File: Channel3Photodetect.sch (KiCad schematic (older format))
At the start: 7 parts, among them U201 MCP6404, U202 LM339

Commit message: revised feedback resistor and updated reference voltage divider
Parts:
- removed R402: 22M, Resistors_SMD:R_0805_HandSoldering, symbol R_Small
- C401: value 2.2p -> 50p
- R401: value 22M -> 2M; Fieldname (none) -> Value; MPN RMCF0805FT22M0 -> (none)
- renumbered R403 to R402
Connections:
- net at C401.1, R402.2, U201.8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: now also R401.1
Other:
- moved on the sheet: R401
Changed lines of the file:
@@
 P 5540 1890
 F 0 "C401" V 5660 1850 50  0000 L CNN
-F 1 "2.2p" V 5430 1760 50  0000 L CNN
+F 1 "50p" V 5430 1760 50  0000 L CNN
 F 2 "Capacitors_SMD:C_0805_HandSoldering" H 5540 1890 50  0001 C CNN
 F 3 "" H 5540 1890 50  0000 C CNN
@@
 	5130 3040 5130 3340
 $Comp
-L R_Small R403
+L R_Small R402
 U 1 1 5822948B
 P 5940 3340
-F 0 "R403" V 6020 3300 50  0000 L CNN
+F 0 "R402" V 6020 3300 50  0000 L CNN
 F 1 "10K" V 5870 3220 50  0000 L CNN
 F 2 "Resistors_SMD:R_0805_HandSoldering" H 5940 3340 50  0001 C CNN
@@
 L R_Small R401
 U 1 1 5823C8F8
-P 5310 2380
-F 0 "R401" V 5390 2340 50  0000 L CNN
-F 1 "22M" V 5240 2260 50  0000 L CNN
-F 2 "Resistors_SMD:R_0805_HandSoldering" H 5310 2380 50  0001 C CNN
-F 3 "" H 5310 2380 50  0000 C CNN
-F 4 "RMCF0805FT22M0" H 5310 2380 60  0001 C CNN "MPN"
-	1    5310 2380
-	0    1    1    0
-$EndComp
-$Comp
-L R_Small R402
-U 1 1 5823C900
-P 5640 2380
-F 0 "R402" V 5720 2340 50  0000 L CNN
-F 1 "22M" V 5570 2260 50  0000 L CNN
-F 2 "Resistors_SMD:R_0805_HandSoldering" H 5640 2380 50  0001 C CNN
-F 3 "" H 5640 2380 50  0000 C CNN
-F 4 "RMCF0805FT22M0" H 5640 2380 60  0001 C CNN "MPN"
-	1    5640 2380
+P 5550 2380
+F 0 "R401" V 5630 2340 50  0000 L CNN
+F 1 "2M" V 5480 2260 50  0000 L CNN
+F 2 "Resistors_SMD:R_0805_HandSoldering" H 5550 2380 50  0001 C CNN
+F 3 "" H 5550 2380 50  0000 C CNN
+F 4 "Value" H 5550 2380 60  0001 C CNN "Fieldname"
+	1    5550 2380
 	0    1    1    0
 $EndComp
 Wire Wire Line
-	5740 2380 5940 2380
+	5940 2380 5650 2380
 Wire Wire Line
-	5540 2380 5410 2380
-Wire Wire Line
-	5210 2380 5130 2380
+	5450 2380 5130 2380
 Connection ~ 5940 2380
 Connection ~ 5130 2380

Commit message: added pull-up resistors
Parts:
- added R403: 10K, Resistors_SMD:R_0805_HandSoldering, symbol R_Small
- R401: Fieldname Value -> (none); MPN (none) -> RC0805FR-072ML
- U202: MPN (none) -> LM339DE4
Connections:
- net PD3: now also R403.1
- new net +3V: R403.2
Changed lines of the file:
@@
 F 2 "Housings_SOIC:SOIC-14_3.9x8.7mm_Pitch1.27mm" H 6740 3140 50  0001 C CNN
 F 3 "" H 6840 3240 50  0000 C CNN
+F 4 "LM339DE4" H 6790 3040 60  0001 C CNN "MPN"
 	3    6790 3040
 	1    0    0    -1
@@
 F 2 "Resistors_SMD:R_0805_HandSoldering" H 5550 2380 50  0001 C CNN
 F 3 "" H 5550 2380 50  0000 C CNN
-F 4 "Value" H 5550 2380 60  0001 C CNN "Fieldname"
+F 4 "RC0805FR-072ML" H 5550 2380 60  0001 C CNN "MPN"
 	1    5550 2380
 	0    1    1    0
@@
 Connection ~ 5940 2380
 Connection ~ 5130 2380
+$Comp
+L R_Small R403
+U 1 1 5824D4E1
+P 7280 2790
+F 0 "R403" V 7360 2750 50  0000 L CNN
+F 1 "10K" V 7210 2670 50  0000 L CNN
+F 2 "Resistors_SMD:R_0805_HandSoldering" H 7280 2790 50  0001 C CNN
+F 3 "" H 7280 2790 50  0000 C CNN
+F 4 "RC0805FR-072ML" H 7280 2790 60  0001 C CNN "MPN"
+	1    7280 2790
+	-1   0    0    1
+$EndComp
+Text GLabel 7280 2540 1    60   Input ~ 0
++3V
+Wire Wire Line
+	7280 2540 7280 2690
+Wire Wire Line
+	7280 2890 7280 3040
+Connection ~ 7280 3040
 $EndSCHEMATC

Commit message: removed 10K resistors used as load for op amps
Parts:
- removed R402: 10K, Resistors_SMD:R_0805_HandSoldering, symbol R_Small
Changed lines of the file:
@@
 	5440 1890 5130 1890
-Wire Wire Line
-	5940 1890 5940 3240
 Wire Wire Line
 	5730 2940 6490 2940
@@
 	5640 1890 5940 1890
 $Comp
-L GND #PWR015
+L GND #PWR013
 U 1 1 58229483
 P 5130 3340
-F 0 "#PWR015" H 5130 3090 50  0001 C CNN
+F 0 "#PWR013" H 5130 3090 50  0001 C CNN
 F 1 "GND" H 5130 3190 50  0000 C CNN
 F 2 "" H 5130 3340 50  0000 C CNN
@@
 Wire Wire Line
 	5130 3040 5130 3340
-$Comp
-L R_Small R402
-U 1 1 5822948B
-P 5940 3340
-F 0 "R402" V 6020 3300 50  0000 L CNN
-F 1 "10K" V 5870 3220 50  0000 L CNN
-F 2 "Resistors_SMD:R_0805_HandSoldering" H 5940 3340 50  0001 C CNN
-F 3 "" H 5940 3340 50  0000 C CNN
-F 4 "Value" H 5940 3340 60  0001 C CNN "Fieldname"
-	1    5940 3340
-	-1   0    0    1
-$EndComp
-Connection ~ 5940 2940
-$Comp
-L GND #PWR016
-U 1 1 58229493
-P 5940 3540
-F 0 "#PWR016" H 5940 3290 50  0001 C CNN
-F 1 "GND" H 5940 3390 50  0000 C CNN
-F 2 "" H 5940 3540 50  0000 C CNN
-F 3 "" H 5940 3540 50  0000 C CNN
-	1    5940 3540
-	1    0    0    -1
-$EndComp
-Wire Wire Line
-	5940 3440 5940 3540
 $Comp
 L VBPW34SR PD401
@@
 	4520 2840 5130 2840
 $Comp
-L GND #PWR017
+L GND #PWR014
 U 1 1 582294D5
 P 4570 3300
-F 0 "#PWR017" H 4570 3050 50  0001 C CNN
+F 0 "#PWR014" H 4570 3050 50  0001 C CNN
 F 1 "GND" H 4570 3150 50  0000 C CNN
 F 2 "" H 4570 3300 50  0000 C CNN
@@
 Wire Wire Line
 	5450 2380 5130 2380
-Connection ~ 5940 2380
 Connection ~ 5130 2380
 $Comp
@@
 	7280 2890 7280 3040
 Connection ~ 7280 3040
+Wire Wire Line
+	5940 1890 5940 2940
+Connection ~ 5940 2940
+Connection ~ 5940 2380
 $EndSCHEMATC

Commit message: replaced potentiometer with trimpot
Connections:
- net GND: now also U201.6 (-); no longer U201.9 (-)
- net at C401.1, R401.1, U202.11 (+): now also U201.7; no longer U201.8
- net at C401.2, PD401.1 (K), R401.2: now also U201.5 (+); no longer U201.10 (+)
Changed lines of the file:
@@
 $Comp
 L MCP6404 U201
-U 3 1 58229472
+U 2 1 58229472
 P 5430 2940
 F 0 "U201" H 5480 3140 50  0000 C CNN
@@
 F 2 "Housings_SOIC:SOIC-14_3.9x8.7mm_Pitch1.27mm" H 5380 3040 50  0001 C CNN
 F 3 "" H 5480 3140 50  0000 C CNN
-	3    5430 2940
+	2    5430 2940
 	1    0    0    -1
 $EndComp

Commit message: completed pcb basic layout
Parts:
- renumbered R403 to R402
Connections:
- net GND: now also U201.9 (-); no longer U201.6 (-)
- net at C401.1, R401.1, U202.11 (+): now also U201.8; no longer U201.7
- net at C401.2, PD401.1 (K), R401.2: now also U201.10 (+); no longer U201.5 (+)
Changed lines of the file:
@@
 $Comp
 L MCP6404 U201
-U 2 1 58229472
+U 3 1 58229472
 P 5430 2940
 F 0 "U201" H 5480 3140 50  0000 C CNN
@@
 F 2 "Housings_SOIC:SOIC-14_3.9x8.7mm_Pitch1.27mm" H 5380 3040 50  0001 C CNN
 F 3 "" H 5480 3140 50  0000 C CNN
-	2    5430 2940
+	3    5430 2940
 	1    0    0    -1
 $EndComp
@@
 	5640 1890 5940 1890
 $Comp
-L GND #PWR013
+L GND #PWR402
 U 1 1 58229483
 P 5130 3340
-F 0 "#PWR013" H 5130 3090 50  0001 C CNN
+F 0 "#PWR402" H 5130 3090 50  0001 C CNN
 F 1 "GND" H 5130 3190 50  0000 C CNN
 F 2 "" H 5130 3340 50  0000 C CNN
@@
 	4520 2840 5130 2840
 $Comp
-L GND #PWR014
+L GND #PWR401
 U 1 1 582294D5
 P 4570 3300
-F 0 "#PWR014" H 4570 3050 50  0001 C CNN
+F 0 "#PWR401" H 4570 3050 50  0001 C CNN
 F 1 "GND" H 4570 3150 50  0000 C CNN
 F 2 "" H 4570 3300 50  0000 C CNN
@@
 Connection ~ 5130 2380
 $Comp
-L R_Small R403
+L R_Small R402
 U 1 1 5824D4E1
 P 7280 2790
-F 0 "R403" V 7360 2750 50  0000 L CNN
+F 0 "R402" V 7360 2750 50  0000 L CNN
 F 1 "10K" V 7210 2670 50  0000 L CNN
 F 2 "Resistors_SMD:R_0805_HandSoldering" H 7280 2790 50  0001 C CNN

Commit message: changed photodiodes to BPW 34 S due to availability. Changed feedbak resistor and cap due to increased current output of diode.
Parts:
- C401: value 50p -> 100p
- PD401: value VBPW34S -> BPW 34 S-Z; AltPart (none) -> VBPW34S
- R401: value 2M -> 1M; Fieldname (none) -> Value; MPN RC0805FR-072ML -> (none)
- R402: Fieldname (none) -> Value; MPN RC0805FR-072ML -> (none)
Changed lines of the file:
@@
 P 5540 1890
 F 0 "C401" V 5660 1850 50  0000 L CNN
-F 1 "50p" V 5430 1760 50  0000 L CNN
+F 1 "100p" V 5430 1760 50  0000 L CNN
 F 2 "Capacitors_SMD:C_0805_HandSoldering" H 5540 1890 50  0001 C CNN
 F 3 "" H 5540 1890 50  0000 C CNN
@@
 	5640 1890 5940 1890
 $Comp
-L GND #PWR402
+L GND #PWR013
 U 1 1 58229483
 P 5130 3340
-F 0 "#PWR402" H 5130 3090 50  0001 C CNN
+F 0 "#PWR013" H 5130 3090 50  0001 C CNN
 F 1 "GND" H 5130 3190 50  0000 C CNN
 F 2 "" H 5130 3340 50  0000 C CNN
@@
 P 4520 3050
 F 0 "PD401" H 4440 3130 50  0000 L CNN
-F 1 "VBPW34S" H 4370 2970 50  0000 L CNN
+F 1 "BPW 34 S-Z" H 4370 2970 50  0000 L CNN
 F 2 "DasBlinkinput:VBPW34S" V 4520 3050 50  0001 C CNN
-F 3 "http://www.vishay.com/docs/81128/vbpw34s.pdf" V 4520 3050 50  0001 C CNN
+F 3 "http://media.digikey.com/pdf/Data%20Sheets/Osram%20PDFs/bpw34_spdf.pdf" V 4520 3050 50  0001 C CNN
 F 4 "Value" H 4520 3050 60  0001 C CNN "Fieldname"
+F 5 "VBPW34S" H 4520 3050 60  0001 C CNN "AltPart"
 	1    4520 3050
 	0    1    1    0
@@
 	4520 2840 5130 2840
 $Comp
-L GND #PWR401
+L GND #PWR014
 U 1 1 582294D5
 P 4570 3300
-F 0 "#PWR401" H 4570 3050 50  0001 C CNN
+F 0 "#PWR014" H 4570 3050 50  0001 C CNN
 F 1 "GND" H 4570 3150 50  0000 C CNN
 F 2 "" H 4570 3300 50  0000 C CNN
@@
 P 5550 2380
 F 0 "R401" V 5630 2340 50  0000 L CNN
-F 1 "2M" V 5480 2260 50  0000 L CNN
+F 1 "1M" V 5480 2260 50  0000 L CNN
 F 2 "Resistors_SMD:R_0805_HandSoldering" H 5550 2380 50  0001 C CNN
 F 3 "" H 5550 2380 50  0000 C CNN
-F 4 "RC0805FR-072ML" H 5550 2380 60  0001 C CNN "MPN"
+F 4 "Value" H 5550 2380 60  0001 C CNN "Fieldname"
+F 5 "   " H 5550 2380 60  0001 C CNN "MPN"
 	1    5550 2380
 	0    1    1    0
@@
 F 2 "Resistors_SMD:R_0805_HandSoldering" H 7280 2790 50  0001 C CNN
 F 3 "" H 7280 2790 50  0000 C CNN
-F 4 "RC0805FR-072ML" H 7280 2790 60  0001 C CNN "MPN"
+F 4 "Value" H 7280 2790 60  0001 C CNN "Fieldname"
 	1    7280 2790
 	-1   0    0    1

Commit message: added test points at outputs of op-amps
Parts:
- added P401: CONN_01X01, Pin_Headers:Pin_Header_Straight_1x01, symbol CONN_01X01
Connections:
- net at C401.1, R401.1, U201.8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: now also P401.1 (P1)
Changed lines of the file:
@@
 	1    0    0    -1
 $EndComp
-Wire Wire Line
-	5130 1890 5130 2840
-Wire Wire Line
-	5440 1890 5130 1890
-Wire Wire Line
-	5730 2940 6490 2940
-Wire Wire Line
-	5640 1890 5940 1890
 $Comp
 L GND #PWR013
@@
 	1    0    0    -1
 $EndComp
-Wire Wire Line
-	5130 3040 5130 3340
 $Comp
 L VBPW34SR PD401
@@
 	0    1    1    0
 $EndComp
-Wire Wire Line
-	4520 2950 4520 2840
-Wire Wire Line
-	4520 2840 5130 2840
 $Comp
 L GND #PWR014
@@
 	1    0    0    -1
 $EndComp
-Wire Wire Line
-	4520 3150 4520 3300
-Wire Wire Line
-	4520 3300 4570 3300
 $Comp
 L LM339 U202
@@
 Text HLabel 6430 3810 0    60   Input ~ 0
 REF_V
-Wire Wire Line
-	6480 3810 6480 3140
-Wire Wire Line
-	6430 3810 6480 3810
-Wire Wire Line
-	6480 3140 6490 3140
 Text HLabel 7400 3040 2    60   Input ~ 0
 PD3
-Wire Wire Line
-	7090 3040 7400 3040
 $Comp
 L R_Small R401
@@
 	0    1    1    0
 $EndComp
-Wire Wire Line
-	5940 2380 5650 2380
-Wire Wire Line
-	5450 2380 5130 2380
-Connection ~ 5130 2380
 $Comp
 L R_Small R402
@@
 Text GLabel 7280 2540 1    60   Input ~ 0
 +3V
+$Comp
+L CONN_01X01 P401
+U 1 1 585446A7
+P 6150 3230
+F 0 "P401" H 6110 3330 50  0000 C CNN
+F 1 "CONN_01X01" V 6250 3230 50  0000 C CNN
+F 2 "Pin_Headers:Pin_Header_Straight_1x01" H 6150 3230 50  0001 C CNN
+F 3 "" H 6150 3230 50  0000 C CNN
+	1    6150 3230
+	0    1    1    0
+$EndComp
+Wire Wire Line
+	5130 1890 5130 2840
+Wire Wire Line
+	5440 1890 5130 1890
+Wire Wire Line
+	5730 2940 6490 2940
+Wire Wire Line
+	5640 1890 5940 1890
+Wire Wire Line
+	5130 3040 5130 3340
+Wire Wire Line
+	4520 2950 4520 2840
+Wire Wire Line
+	4520 2840 5130 2840
+Wire Wire Line
+	4520 3150 4520 3300
+Wire Wire Line
+	4520 3300 4570 3300
+Wire Wire Line
+	6480 3810 6480 3140
+Wire Wire Line
+	6430 3810 6480 3810
+Wire Wire Line
+	6480 3140 6490 3140
+Wire Wire Line
+	7090 3040 7400 3040
+Wire Wire Line
+	5940 2380 5650 2380
+Wire Wire Line
+	5450 2380 5130 2380
+Connection ~ 5130 2380
 Wire Wire Line
 	7280 2540 7280 2690
@@
 Connection ~ 5940 2940
 Connection ~ 5940 2380
+Wire Wire Line
+	6150 3030 6150 2940
+Connection ~ 6150 2940
 $EndSCHEMATC

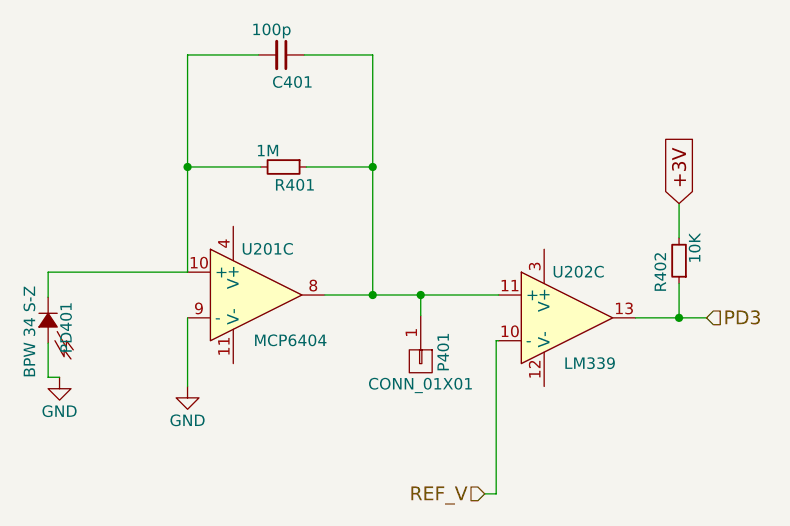
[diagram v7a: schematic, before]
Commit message: corrected inputs on opamp and rerouted traces
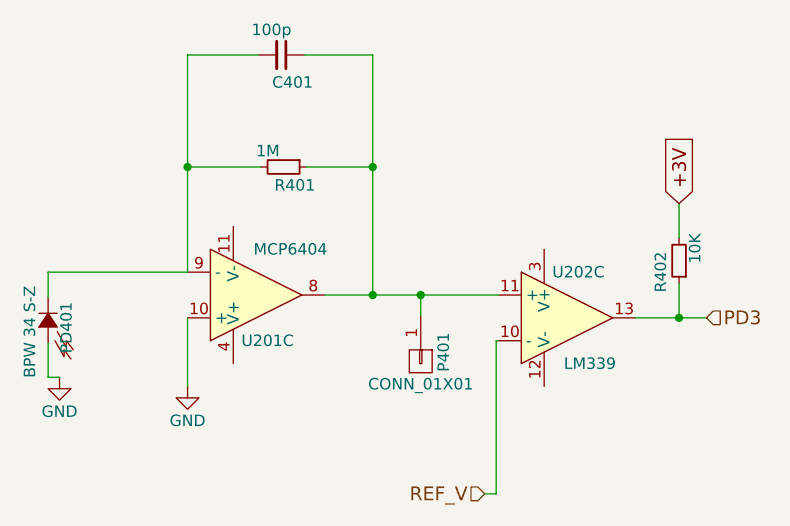
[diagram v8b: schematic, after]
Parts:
- U201, U202: footprint Housings_SOIC:SOIC-14_3.9x8.7mm_Pitch1.27mm -> DasBlinkinput:SOIC-14_3.9x8.7mm_Pitch1.27mm
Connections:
- net GND: now also U201.10 (+); no longer U201.9 (-)
- net at C401.2, PD401.1 (K), R401.2: now also U201.9 (-); no longer U201.10 (+)
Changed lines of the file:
@@
 F 0 "U201" H 5480 3140 50  0000 C CNN
 F 1 "MCP6404" H 5580 2740 50  0000 C CNN
-F 2 "Housings_SOIC:SOIC-14_3.9x8.7mm_Pitch1.27mm" H 5380 3040 50  0001 C CNN
+F 2 "DasBlinkinput:SOIC-14_3.9x8.7mm_Pitch1.27mm" H 5380 3040 50  0001 C CNN
 F 3 "" H 5480 3140 50  0000 C CNN
 	3    5430 2940
-	1    0    0    -1
+	1    0    0    1
 $EndComp
 $Comp
@@
 F 0 "U202" H 6840 3240 50  0000 C CNN
 F 1 "LM339" H 6890 2840 50  0000 C CNN
-F 2 "Housings_SOIC:SOIC-14_3.9x8.7mm_Pitch1.27mm" H 6740 3140 50  0001 C CNN
+F 2 "DasBlinkinput:SOIC-14_3.9x8.7mm_Pitch1.27mm" H 6740 3140 50  0001 C CNN
 F 3 "" H 6840 3240 50  0000 C CNN
 F 4 "LM339DE4" H 6790 3040 60  0001 C CNN "MPN"
